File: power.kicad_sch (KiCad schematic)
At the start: 1 part, among them U2 AG9905-LP

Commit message: Adding ethernet module and more
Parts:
- added C1, C3: C, symbol Device:C
- added C2: C_Polarized, symbol Device:C_Polarized
- added C7: 10uF, symbol Device:C_Polarized
- added C8: 4u7F, symbol Device:C_Polarized
- added D1: SMAJ58A, Diode_SMD:D_SMA, symbol Diode:SMAJ58A
- added FB1, FB2, FB3, FB4, FB5, FB6, FB7: FerriteBead, Inductor_SMD:L_0603_1608Metric, symbol Device:FerriteBead
- added R3: 0R, Resistor_SMD:R_0201_0603Metric, symbol Device:R
- added U10, U6, U9: MAX40200AUK, Package_TO_SOT_SMD:SOT-23-5, symbol Analog_Switch:MAX40200AUK
- added U11: B2403S-1WR3, 1_Custom_Rick:B2403S-1WR3, symbol Rick:B2403S-1WR3
- added U14: NCP1117-3.3_TO252, Package_TO_SOT_SMD:TO-252-2, symbol Regulator_Linear:NCP1117-3.3_TO252
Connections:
- net GND: now also C7.2, C8.2, R3.2, U10.2 (GND), U11.1 (-Vin), U14.1 (GND), U6.2 (GND), U9.2 (GND)
- net VIN+: now also FB3.2
- net VIN-: now also FB6.2
- net VN_PoE: now also D1.2 (A2), FB4.1
- net VP12V: now also U11.2 (+Vin)
- net VP3V3: now also C8.1, U14.2 (VO)
- net VP5V: now also C7.1, U10.5 (OUT), U14.3 (VI), U6.5 (OUT), U9.5 (OUT)
- net VP_PoE: now also D1.1 (A1), FB1.1
- net VP_USB: now also U10.1 (VDD), U10.3 (EN)
- net at U2.1 (+VDC), U2.2 (+VDC): now also C1.1, C2.1, FB7.1
- net at U2.3 (-VDC): now also C1.2, C2.2, C3.2
- new net: C3.1, FB7.2, U6.1 (VDD), U6.3 (EN)
- new net: R3.1, U11.3 (-Vout)
- new net: U11.4 (+Vout), U9.1 (VDD), U9.3 (EN)
- new net: FB5.2, FB6.1
- new net: FB1.2, FB2.1
- new net: FB2.2, FB3.1
- new net: FB4.2, FB5.1
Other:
- note added: "4.48V"
- note added: "5.65V"
- note added: "C1 = 10µF 25V C2 = 100uF 25V C3, C4 = 4.7nF 2KV D1 = SMAJ58A RB = ≥ I load min BR1 & BR2 = MB4S L1 – L6 = MMZ2012S102A"
- note added: "Cin 10 F ceramic or tantalum"
- note added: "Cout and its use is mandatory to ensure output stability. A minimum capacitance value of 4.7 F with an equivalent series resistance (ESR) that is within the limits of 33 m (typ) to 2.2 is required"
- note added: "Increasing the output voltage, connect R between ADJ and -VDC"
- note added: "Max continuous 1.4A @5VDC (7W)"
- note added: "Reducing the output voltage, connect R between ADJ and +VDC"
- note added: "When disabled (EN = low) blocks up to 6V"
- note added: "Wrong version this is 24 to 3.3 need 12 to 5v"
- note removed: "Ag9905-LP"
- note removed: "Diode bridge in connector"
- note removed: "USB-C in 2pin 1.5mm in 12vdc to 5vdc converter lcsc PoE input after 5v so with ideal diode for usbc and 5v out protection 3v3 ldo to esp32"
- moved on the sheet: U2

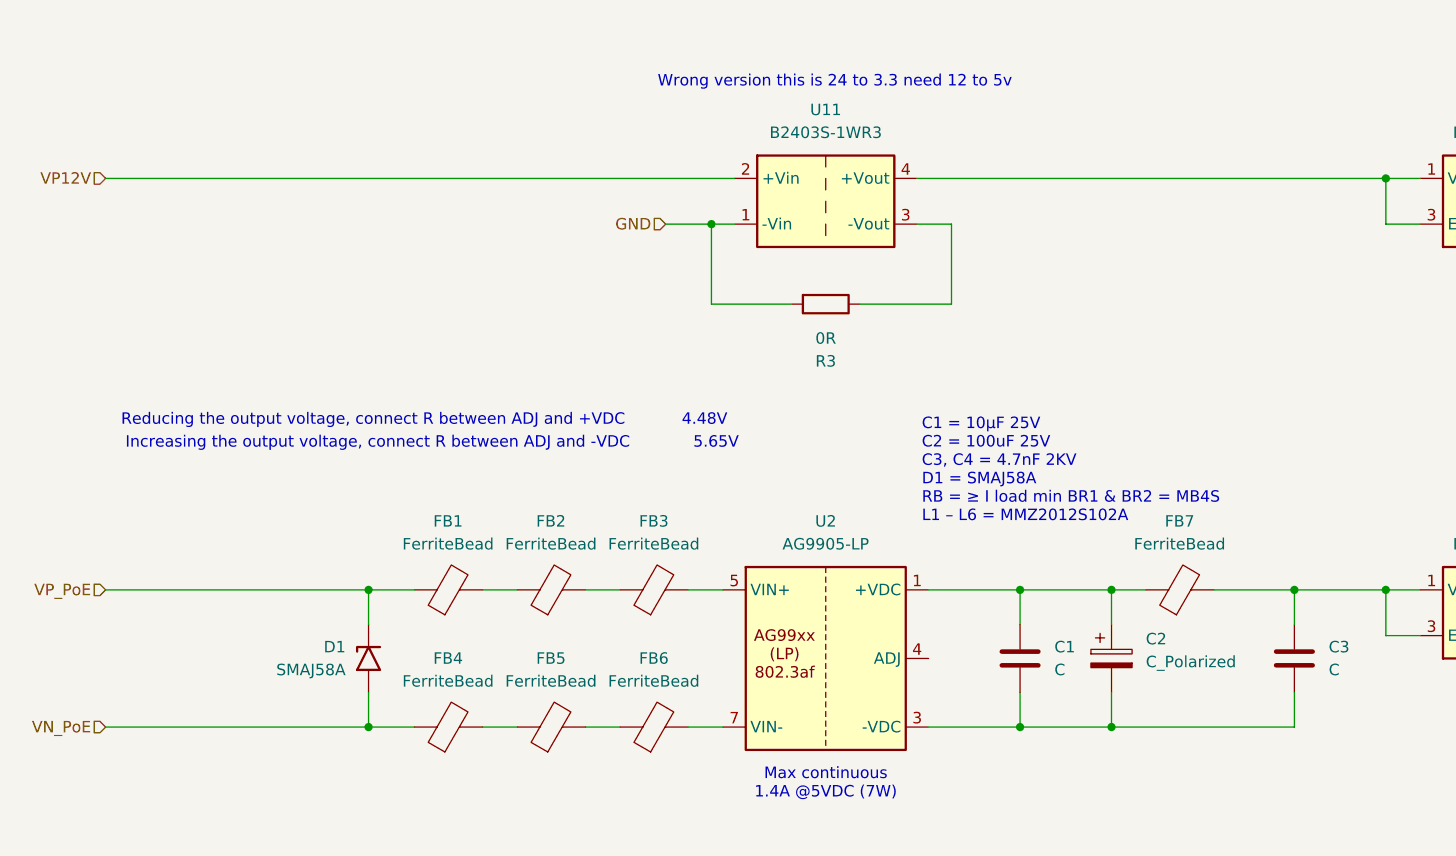
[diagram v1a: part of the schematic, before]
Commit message: Ethernet progress, 40pin connector, save progress
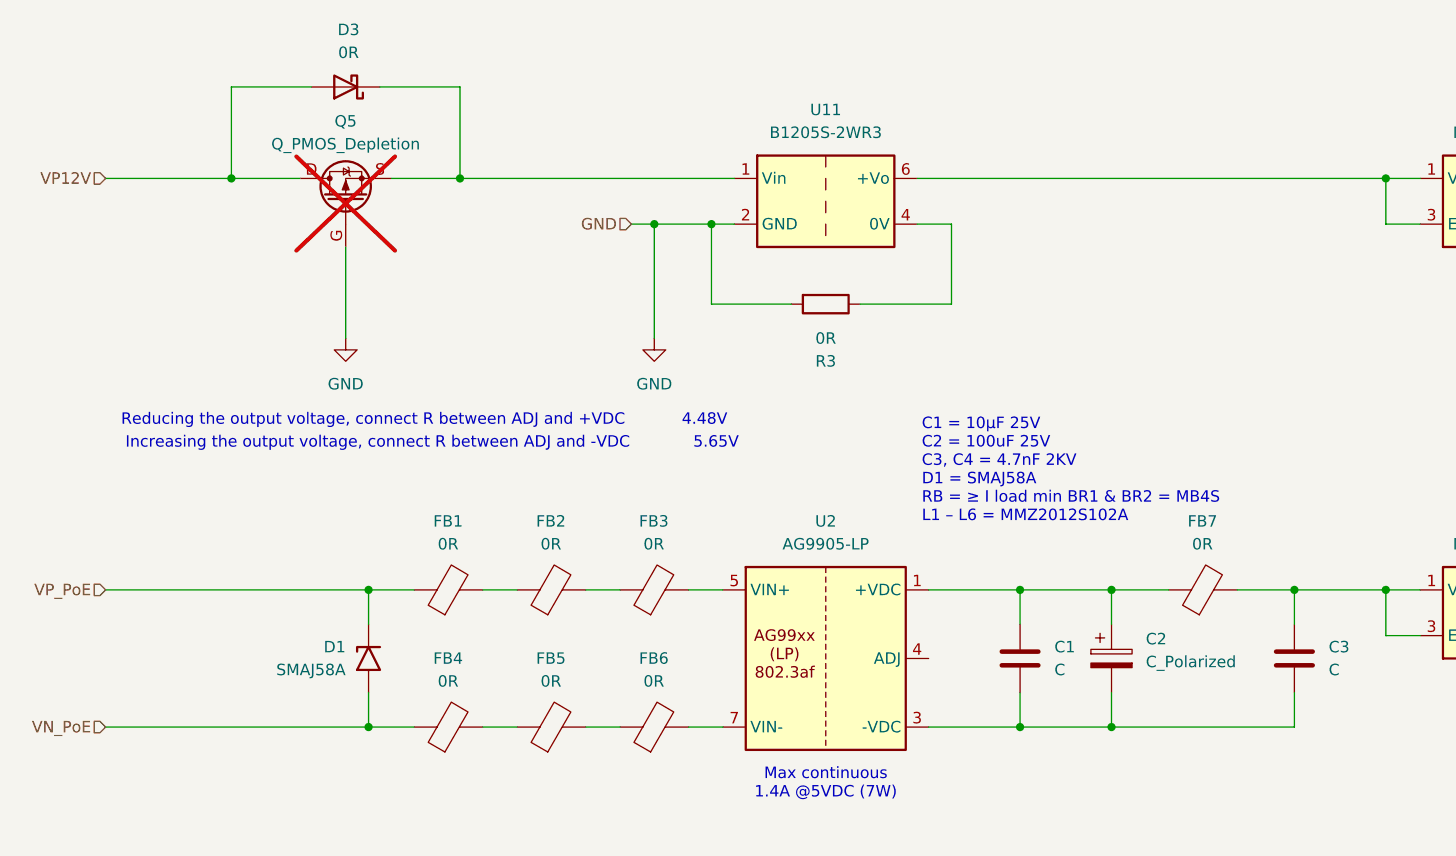
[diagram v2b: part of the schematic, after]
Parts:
- removed U11: B2403S-1WR3, 1_Custom_Rick:B2403S-1WR3, symbol Rick:B2403S-1WR3
- added D3: 0R, Diode_SMD:D_0603_1608Metric, symbol Device:D_Schottky
- added Q5: Q_PMOS_Depletion, symbol Device:Q_PMOS_Depletion
- added U11: B1205S-2WR3, symbol Rick:B1205S-2WR3
- FB1, FB2, FB3, FB4, FB5, FB6, FB7: value FerriteBead -> 0R
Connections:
- net GND: now also Q5.G, U11.2 (GND)
- net VP12V: now also D3.2 (A), Q5.D
- net at R3.1: now also U11.4 (0V)
- net at U9.1 (VDD), U9.3 (EN): now also U11.6 (+Vo)
- new net: D3.1 (K), Q5.S, U11.1 (Vin)
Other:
- note removed: "Wrong version this is 24 to 3.3 need 12 to 5v"
- moved on the sheet: FB7

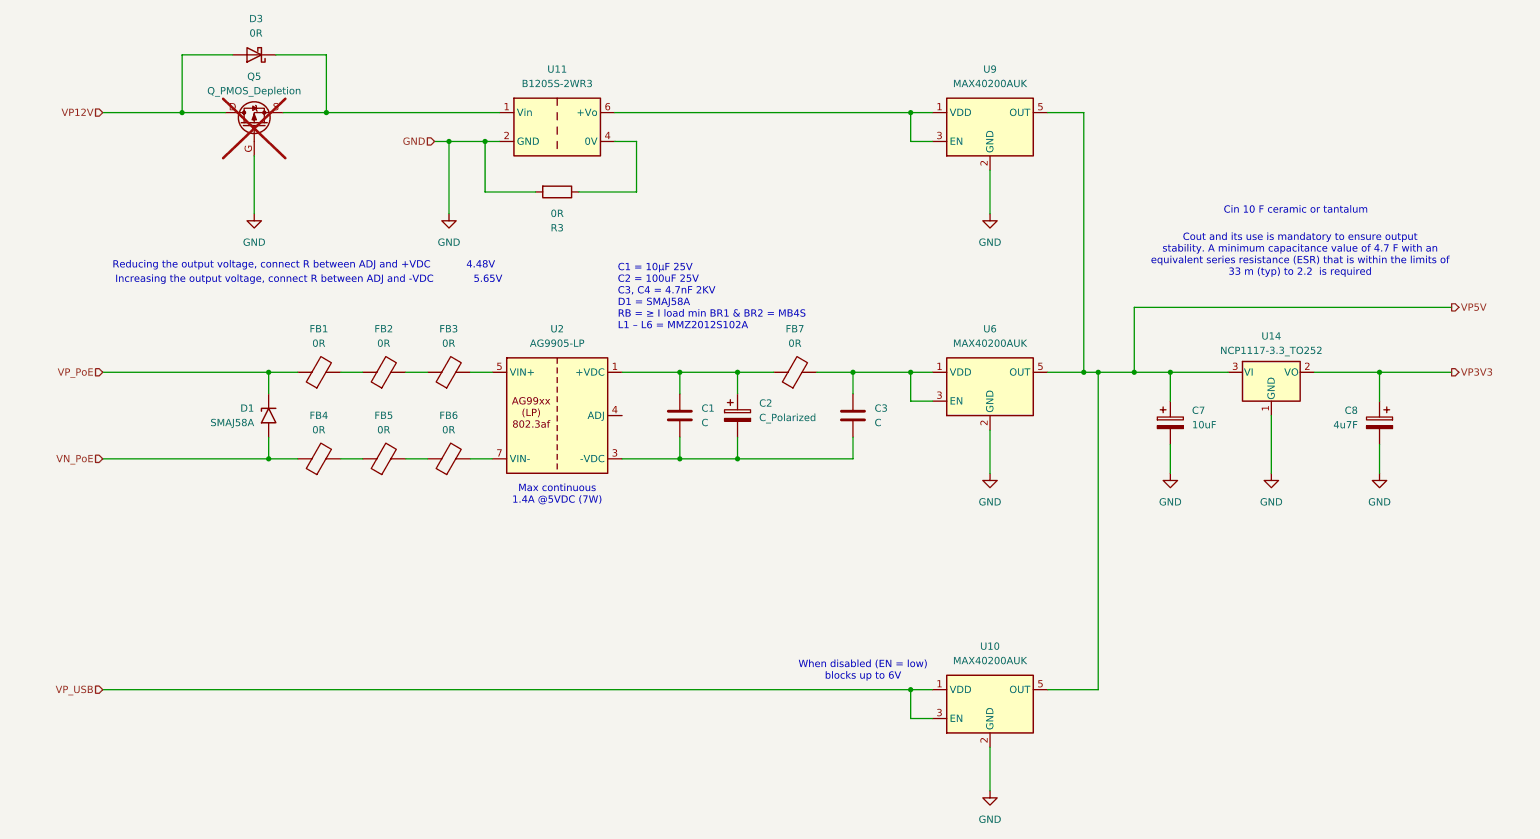
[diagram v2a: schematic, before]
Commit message: NMEA0183 and NMEA2000 schematics
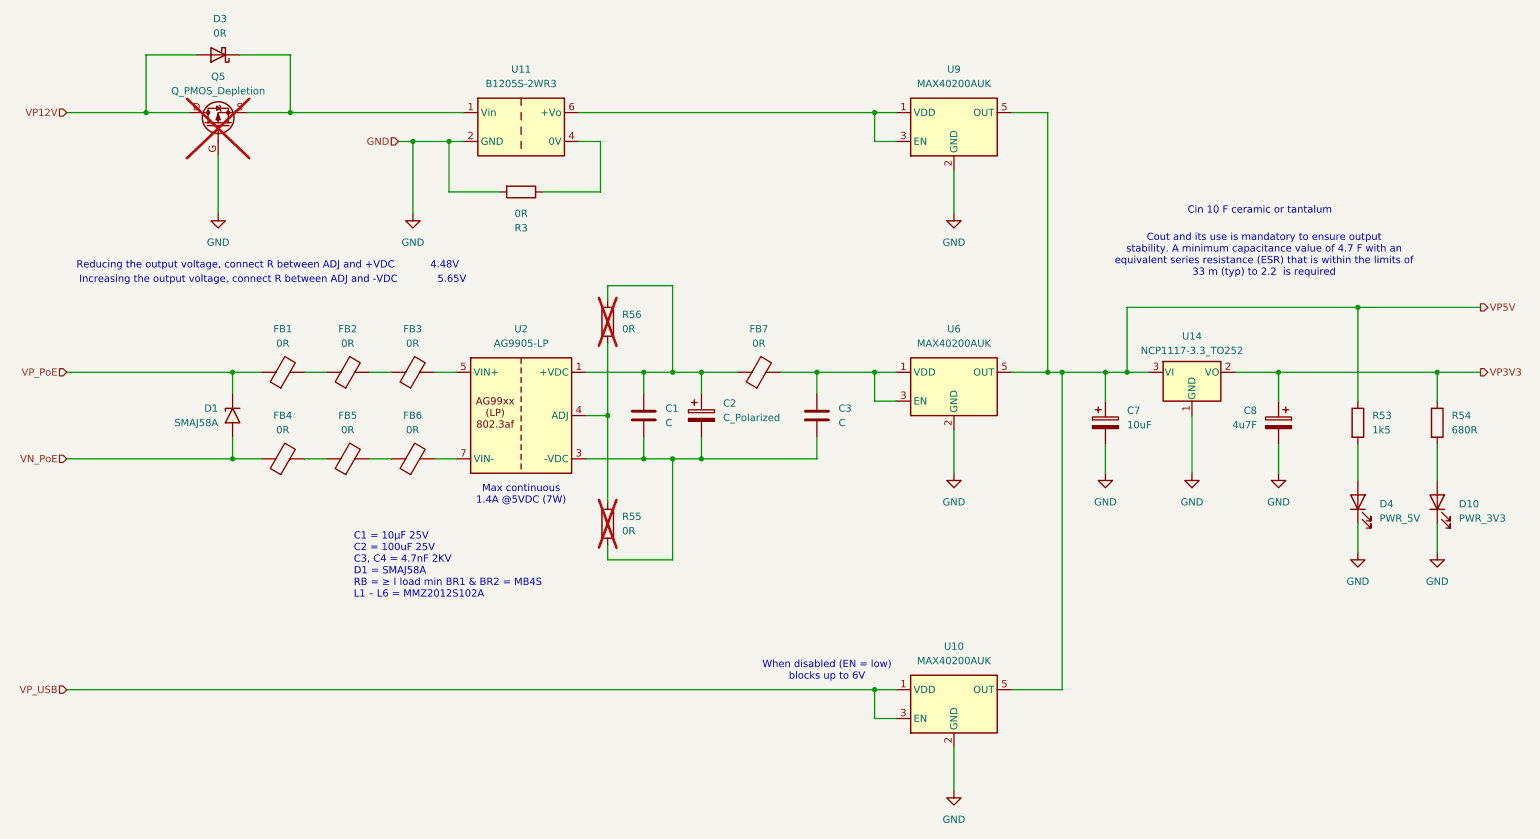
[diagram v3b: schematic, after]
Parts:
- added D10: PWR_3V3, LED_SMD:LED_0603_1608Metric, symbol Device:LED
- added D4: PWR_5V, LED_SMD:LED_0603_1608Metric, symbol Device:LED
- added R53: 1k5, Resistor_SMD:R_0603_1608Metric, symbol Device:R
- added R54: 680R, Resistor_SMD:R_0603_1608Metric, symbol Device:R
- added R55, R56: 0R, Resistor_SMD:R_0603_1608Metric, symbol Device:R
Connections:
- net GND: now also D10.1 (K), D4.1 (K)
- net VP3V3: now also R54.1
- net VP5V: now also R53.1
- net at C1.1, C2.1, FB7.1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: now also R56.1
- net at C1.2, C2.2, C3.2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: now also R55.2
- net at U2.4 (ADJ): now also R55.1, R56.2
- new net: D4.2 (A), R53.2
- new net: D10.2 (A), R54.2
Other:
- moved on the sheet: C1, C2, C3, C7, C8, D1, D3, FB1, FB2, FB3, FB4, FB5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

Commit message: Clean up and testpoints
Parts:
- added TP22, TP23, TP24: TestPoint, TestPoint:TestPoint_Pad_D1.5mm, symbol Connector:TestPoint
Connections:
- net VP_USB: now also TP24.1
- net at C3.1, FB7.2, U6.1 (VDD)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: now also TP23.1
- net at U11.6 (+Vo), U9.1 (VDD), U9.3 (EN): now also TP22.1

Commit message: Layout save
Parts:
- C1, C2, C3, C7, C8: footprint (none) -> Capacitor_SMD:C_0603_1608Metric
- U11: footprint (none) -> Rick:B1205S-2WR3
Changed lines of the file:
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@@
 			)
 		)
-		(property "Footprint" ""
+		(property "Footprint" "Capacitor_SMD:C_0603_1608Metric"
 			(at 126.6952 93.98 0)
 			(hide yes)
@@
 			)
 		)
-		(property "Footprint" ""
+		(property "Footprint" "Capacitor_SMD:C_0603_1608Metric"
 			(at 236.5248 95.25 0)
 			(hide yes)
@@
 			)
 		)
-		(property "Footprint" ""
+		(property "Footprint" "Capacitor_SMD:C_0603_1608Metric"
 			(at 207.9752 95.25 0)
 			(hide yes)
@@
 			)
 		)
-		(property "Footprint" ""
+		(property "Footprint" "Capacitor_SMD:C_0603_1608Metric"
 			(at 136.8552 93.98 0)
 			(hide yes)
@@
 			)
 		)
-		(property "Footprint" ""
+		(property "Footprint" "Capacitor_SMD:C_0603_1608Metric"
 			(at 157.1752 93.98 0)
 			(hide yes)
@@
 			)
 		)
-		(property "Footprint" ""
+		(property "Footprint" "Rick:B1205S-2WR3"
 			(at 104.14 45.974 0)
 			(hide yes)

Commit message: Power layout started
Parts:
- removed D3: 0R, Diode_SMD:D_0603_1608Metric, symbol Device:D_Schottky
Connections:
- net GND: now also C1.2, C2.2, C3.2, R55.2, U2.3 (-VDC)
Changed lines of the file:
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@@
 	)
 	(junction
-		(at 63.5 36.83)
-		(diameter 0)
-		(color 0 0 0 0)
-	)
-	(junction
 		(at 85.09 41.91)
 		(diameter 0)
@@
 	)
 	(junction
-		(at 156.21 82.55)
+		(at 156.21 97.79)
 		(diameter 0)
 		(color 0 0 0 0)
 	)
 	(junction
-		(at 38.1 36.83)
+		(at 156.21 82.55)
 		(diameter 0)
 		(color 0 0 0 0)
@@
 	)
 	(junction
+		(at 180.34 97.79)
+		(diameter 0)
+		(color 0 0 0 0)
+	)
+	(junction
 		(at 130.81 82.55)
 		(diameter 0)
@@
 	(wire
 		(pts
-			(xy 24.13 36.83) (xy 38.1 36.83)
+			(xy 24.13 36.83) (xy 45.72 36.83)
 		)
 		(stroke
@@
 	(wire
 		(pts
-			(xy 38.1 26.67) (xy 38.1 36.83)
-		)
-		(stroke
-			(width 0)
-			(type default)
-		)
-	)
-	(wire
-		(pts
 			(xy 166.37 41.91) (xy 166.37 36.83)
 		)
@@
 	(wire
 		(pts
-			(xy 180.34 92.71) (xy 180.34 100.33)
+			(xy 180.34 92.71) (xy 180.34 97.79)
 		)
 		(stroke
@@
 	(wire
 		(pts
-			(xy 63.5 26.67) (xy 63.5 36.83)
-		)
-		(stroke
-			(width 0)
-			(type default)
-		)
-	)
-	(wire
-		(pts
 			(xy 135.89 82.55) (xy 142.24 82.55)
 		)
@@
 	(wire
 		(pts
-			(xy 63.5 36.83) (xy 93.98 36.83)
-		)
-		(stroke
-			(width 0)
-			(type default)
-		)
-	)
-	(wire
-		(pts
 			(xy 135.89 86.36) (xy 135.89 82.55)
 		)
@@
 	(wire
 		(pts
-			(xy 54.61 26.67) (xy 63.5 26.67)
-		)
-		(stroke
-			(width 0)
-			(type default)
-		)
-	)
-	(wire
-		(pts
 			(xy 53.34 97.79) (xy 53.34 93.98)
 		)
@@
 	(wire
 		(pts
-			(xy 38.1 36.83) (xy 45.72 36.83)
+			(xy 156.21 97.79) (xy 180.34 97.79)
 		)
 		(stroke
@@
 	(wire
 		(pts
-			(xy 46.99 26.67) (xy 38.1 26.67)
-		)
-		(stroke
-			(width 0)
-			(type default)
-		)
-	)
-	(wire
-		(pts
 			(xy 161.29 82.55) (xy 166.37 82.55)
 		)
@@
 	(wire
 		(pts
-			(xy 55.88 36.83) (xy 63.5 36.83)
+			(xy 55.88 36.83) (xy 93.98 36.83)
 		)
 		(stroke
@@
 	(wire
 		(pts
+			(xy 180.34 97.79) (xy 180.34 100.33)
+		)
+		(stroke
+			(width 0)
+			(type default)
+		)
+	)
+	(wire
+		(pts
 			(xy 82.55 41.91) (xy 85.09 41.91)
 		)
@@
 					(unit 1)
 				)
-			)
-		)
-	)
-	(symbol
-		(lib_id "Device:D_Schottky")
-		(at 50.8 26.67 180)
-		(unit 1)
-		(body_style 1)
-		(exclude_from_sim no)
-		(in_bom yes)
-		(on_board yes)
-		(in_pos_files yes)
-		(dnp no)
-		(fields_autoplaced yes)
-		(property "Reference" "D3"
-			(at 51.1175 20.32 0)
-			(show_name no)
-			(do_not_autoplace no)
-			(effects
-				(font
-					(size 1.27 1.27)
-				)
-			)
-		)
-		(property "Value" "0R"
-			(at 51.1175 22.86 0)
-			(show_name no)
-			(do_not_autoplace no)
-			(effects
-				(font
-					(size 1.27 1.27)
-				)
-			)
-		)
-		(property "Footprint" "Diode_SMD:D_0603_1608Metric"
-			(at 50.8 26.67 0)
-			(hide yes)
-			(show_name no)
-			(do_not_autoplace no)
-			(effects
-				(font
-					(size 1.27 1.27)
-				)
-			)
-		)
-		(property "Datasheet" ""
-			(at 50.8 26.67 0)
-			(hide yes)
-			(show_name no)
-			(do_not_autoplace no)
-			(effects
-				(font
-					(size 1.27 1.27)
-				)
-			)
-		)
-		(property "Description" "Schottky diode"
-			(at 50.8 26.67 0)
-			(hide yes)
-			(show_name no)
-			(do_not_autoplace no)
-			(effects
-				(font
-					(size 1.27 1.27)
-				)
-			)
-		)
-		(pin "1"
-		)
-		(pin "2"
-		)
-		(instances
-			(project "AIS-Converter"
-				(path "/af2e2bda-c8b0-494b-9cbc-4303d4ae7608/129c204b-2a58-4519-abe1-43b32e5912d0"
-					(reference "D3")
-					(unit 1)
-				)
